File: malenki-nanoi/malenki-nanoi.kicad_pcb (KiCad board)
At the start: 4 copper layers, 19 x 32 mm, 45 parts, among them J1 Conn_01x02_Male-Connector, J2 Conn_01x08_Male, J3 Conn_01x02, J4 Conn_01x02_Male-Connector, J5 Conn_01x02_Male-Connector, J6 Conn_01x02_Male-Connector, U1 A7105, U2 AIC1734-33GUTR, U3 ATtiny1616-M, U4 DRV8837DSGR, U5 DRV8837DSGR, U6 DRV8837DSGR, Y1 16 Mhz 20ppm

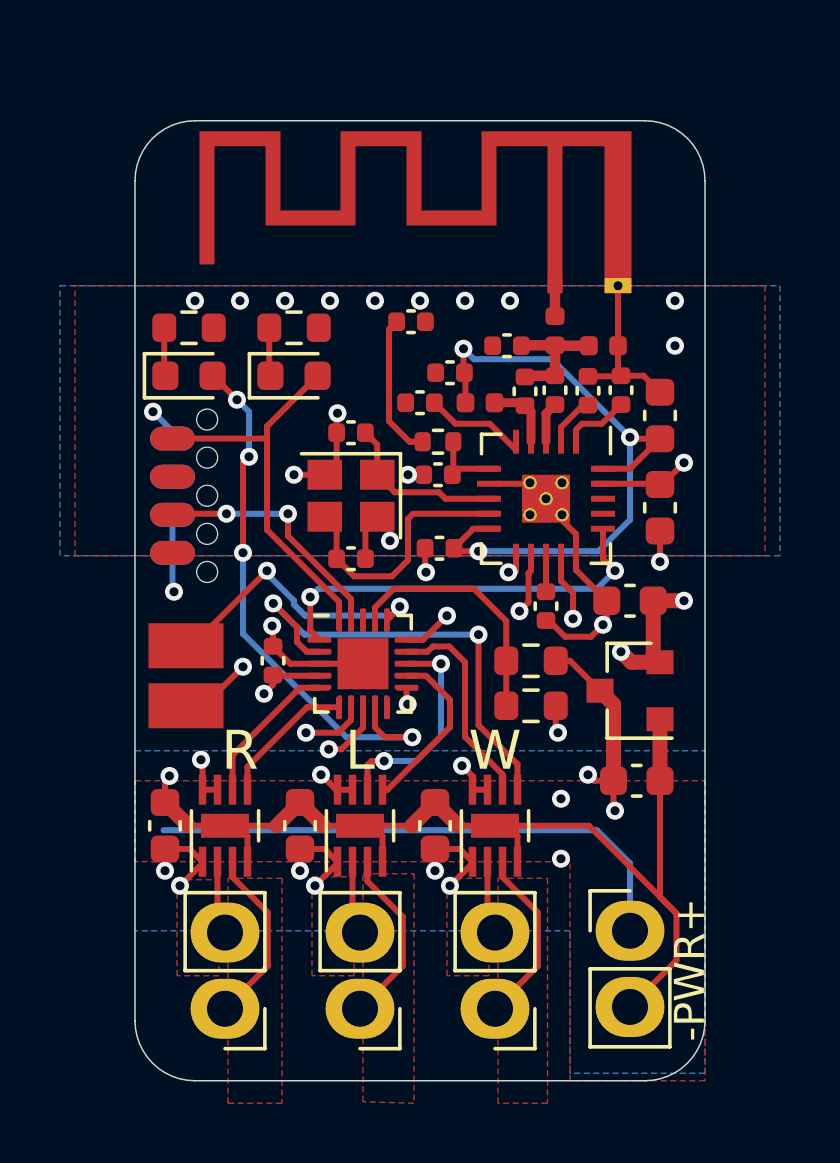
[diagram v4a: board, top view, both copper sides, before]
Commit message: Crystal caps update
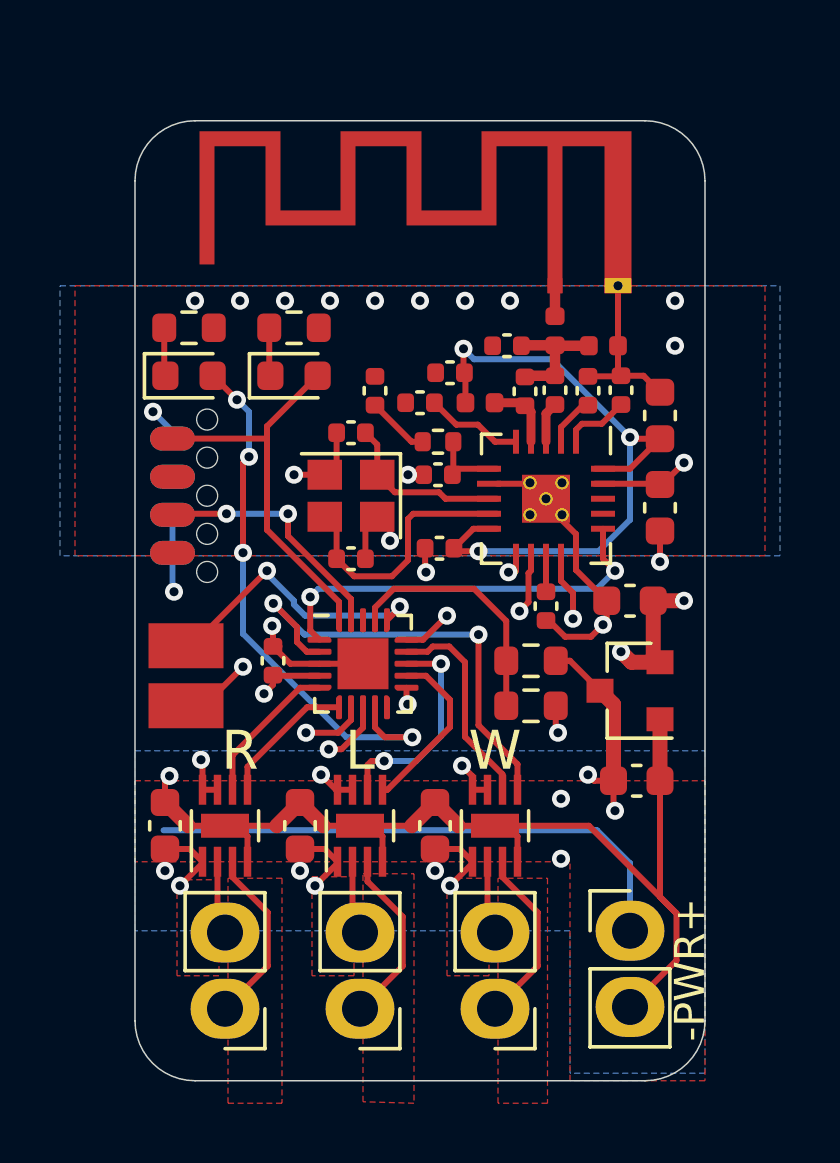
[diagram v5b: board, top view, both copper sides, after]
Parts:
- C14, C15: value 33pF -> 22pF
- R1, R2: value 100R -> 1k
- moved C19 2.59 mm to (96.0, 58.5), turned to 90 degrees
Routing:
- net Net-(C19-Pad1): track 4.83 -> 2.10 mm
- net GND: track 65.8 -> 65.1 mm, vias 23 -> 22
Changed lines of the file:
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@@
     (descr "Resistor SMD 0603 (1608 Metric), square (rectangular) end terminal, IPC_7351 nominal, (Body size source: IPC-SM-782 page 72, https://www.pcb-3d.com/wordpress/wp-content/uploads/ipc-sm-782a_amendment_1_and_2.pdf), generated with kicad-footprint-generator")
     (tags "resistor")
-    (property "LCSC" "C25804")
+    (property "LCSC" "")
     (property "Partnum" "C25804")
     (property "Sheet file" "malenki-nanoi.kicad_sch")
@@
       (effects (font (size 1 1) (thickness 0.15)))
     )
-    (fp_text value "33pF" (at 0 1.16) (layer "F.Fab")
+    (fp_text value "22pF" (at 0 1.16) (layer "F.Fab")
       (effects (font (size 1 1) (thickness 0.15)))
     )
@@
     (descr "Resistor SMD 0603 (1608 Metric), square (rectangular) end terminal, IPC_7351 nominal, (Body size source: IPC-SM-782 page 72, https://www.pcb-3d.com/wordpress/wp-content/uploads/ipc-sm-782a_amendment_1_and_2.pdf), generated with kicad-footprint-generator")
     (tags "resistor")
-    (property "LCSC" "C22775")
+    (property "LCSC" "")
     (property "Partnum" "")
     (property "Sheet file" "malenki-nanoi.kicad_sch")
@@
       (effects (font (size 1 1) (thickness 0.15)))
     )
-    (fp_text value "100R" (at 0 1.43) (layer "F.Fab") hide
+    (fp_text value "1k" (at 0 1.43) (layer "F.Fab") hide
       (effects (font (size 1 1) (thickness 0.15)))
     )
@@
       (effects (font (size 1 1) (thickness 0.15)))
     )
-    (fp_text value "33pF" (at 0 1.16) (layer "F.Fab")
+    (fp_text value "22pF" (at 0 1.16) (layer "F.Fab")
       (effects (font (size 1 1) (thickness 0.15)))
     )
@@
     (descr "Resistor SMD 0402 (1005 Metric), square (rectangular) end terminal, IPC_7351 nominal, (Body size source: IPC-SM-782 page 72, https://www.pcb-3d.com/wordpress/wp-content/uploads/ipc-sm-782a_amendment_1_and_2.pdf), generated with kicad-footprint-generator")
     (tags "resistor")
-    (property "LCSC" "C8218")
+    (property "LCSC" "")
     (property "Sheet file" "radio.kicad_sch")
     (property "Sheet name" "radio")
@@
     (descr "Resistor SMD 0603 (1608 Metric), square (rectangular) end terminal, IPC_7351 nominal, (Body size source: IPC-SM-782 page 72, https://www.pcb-3d.com/wordpress/wp-content/uploads/ipc-sm-782a_amendment_1_and_2.pdf), generated with kicad-footprint-generator")
     (tags "resistor")
-    (property "LCSC" "C4216")
+    (property "LCSC" "")
     (property "Partnum" "C4216")
     (property "Sheet file" "malenki-nanoi.kicad_sch")
@@
     (descr "Resistor SMD 0603 (1608 Metric), square (rectangular) end terminal, IPC_7351 nominal, (Body size source: IPC-SM-782 page 72, https://www.pcb-3d.com/wordpress/wp-content/uploads/ipc-sm-782a_amendment_1_and_2.pdf), generated with kicad-footprint-generator")
     (tags "resistor")
-    (property "LCSC" "C22775")
+    (property "LCSC" "")
     (property "Partnum" "")
     (property "Sheet file" "malenki-nanoi.kicad_sch")
@@
       (effects (font (size 1 1) (thickness 0.15)))
     )
-    (fp_text value "100R" (at 0 1.43) (layer "F.Fab") hide
+    (fp_text value "1k" (at 0 1.43) (layer "F.Fab") hide
       (effects (font (size 1 1) (thickness 0.15)))
     )
@@
   )
   (footprint "Capacitor_SMD:C_0402_1005Metric" (layer "F.Cu")
-    (at 97.2 56.2)
+    (at 96 58.5 90)
     (descr "Capacitor SMD 0402 (1005 Metric), square (rectangular) end terminal, IPC_7351 nominal, (Body size source: IPC-SM-782 page 76, https://www.pcb-3d.com/wordpress/wp-content/uploads/ipc-sm-782a_amendment_1_and_2.pdf), generated with kicad-footprint-generator")
     (tags "capacitor")
@@
     (property "Sheet name" "radio")
     (attr smd)
-    (fp_text reference "C19" (at 0 -1.16) (layer "F.SilkS") hide
-      (effects (font (size 1 1) (thickness 0.15)))
-    )
-    (fp_text value "10nF" (at 0 1.16) (layer "F.Fab")
-      (effects (font (size 1 1) (thickness 0.15)))
-    )
-    (fp_text user "${REFERENCE}" (at 0 0) (layer "F.Fab") hide
+    (fp_text reference "C19" (at 0 -1.16 90) (layer "F.SilkS") hide
+      (effects (font (size 1 1) (thickness 0.15)))
+    )
+    (fp_text value "10nF" (at 0 1.16 90) (layer "F.Fab")
+      (effects (font (size 1 1) (thickness 0.15)))
+    )
+    (fp_text user "${REFERENCE}" (at 0 0 90) (layer "F.Fab") hide
       (effects (font (size 0.25 0.25) (thickness 0.04)))
     )
@@
     (fp_line (start -0.5 0.25) (end -0.5 -0.25) (layer "F.Fab") (width 0.1))
     (fp_line (start 0.5 -0.25) (end 0.5 0.25) (layer "F.Fab") (width 0.1))
-    (pad "1" smd roundrect (at -0.48 0) (size 0.56 0.62) (layers "F.Cu" "F.Paste" "F.Mask") (roundrect_rratio 0.25)
+    (pad "1" smd roundrect (at -0.48 0 90) (size 0.56 0.62) (layers "F.Cu" "F.Paste" "F.Mask") (roundrect_rratio 0.25)
       (net 14 "Net-(C19-Pad1)"))
-    (pad "2" smd roundrect (at 0.48 0) (size 0.56 0.62) (layers "F.Cu" "F.Paste" "F.Mask") (roundrect_rratio 0.25)
+    (pad "2" smd roundrect (at 0.48 0 90) (size 0.56 0.62) (layers "F.Cu" "F.Paste" "F.Mask") (roundrect_rratio 0.25)
       (net 1 "GND"))
     (model "${KISYS3DMOD}/Capacitor_SMD.3dshapes/C_0402_1005Metric.wrl"
@@
   (segment (start 101.133334 61.6) (end 101.166667 61.566667) (width 0.2) (layer "F.Cu") (net 1))
   (segment (start 92.725 73) (end 93.5 72.225) (width 0.5) (layer "F.Cu") (net 1))
-  (segment (start 94.72 59.9) (end 94.72 59.28) (width 0.2) (layer "F.Cu") (net 1))
   (segment (start 103.2 66.7) (end 103.6 66.3) (width 0.2) (layer "F.Cu") (net 1))
   (segment (start 98.775 73) (end 100 73) (width 0.2) (layer "F.Cu") (net 1))
@@
   (segment (start 91.75 74.2) (end 91.75 73.35) (width 0.2) (layer "F.Cu") (net 1))
   (segment (start 93.18 67.6) (end 92.6 67.02) (width 0.2) (layer "F.Cu") (net 1))
-  (segment (start 94.72 59.28) (end 94.75 59.25) (width 0.2) (layer "F.Cu") (net 1))
   (segment (start 92.6 67.02) (end 92.82 67.02) (width 0.2) (layer "F.Cu") (net 1))
   (segment (start 106.05001 75.920097) (end 106.05001 77.48999) (width 0.2) (layer "F.Cu") (net 1))
@@
   (via (at 99 55.5) (size 0.6) (drill 0.3) (layers "F.Cu" "B.Cu") (free) (net 1))
   (via (at 91.5 55.5) (size 0.6) (drill 0.3) (layers "F.Cu" "B.Cu") (free) (net 1))
-  (via (at 94.75 59.25) (size 0.6) (drill 0.3) (layers "F.Cu" "B.Cu") (net 1))
   (via (at 105.5 64.2) (size 0.6) (drill 0.3) (layers "F.Cu" "B.Cu") (net 1))
   (via (at 102.1 69.9) (size 0.6) (drill 0.3) (layers "F.Cu" "B.Cu") (net 1))
@@
   (segment (start 104.5 60.05) (end 101.9 57.45) (width 0.2) (layer "B.Cu") (net 7))
   (segment (start 104.5 60.05) (end 104.5 62.8) (width 0.2) (layer "B.Cu") (net 7))
-  (segment (start 98.68 59.6) (end 97.98 58.9) (width 0.2) (layer "F.Cu") (net 8))
-  (segment (start 100.7 60.475) (end 99.825 59.6) (width 0.2) (layer "F.Cu") (net 8))
-  (segment (start 99.825 59.6) (end 98.68 59.6) (width 0.2) (layer "F.Cu") (net 8))
+  (segment (start 99.42999 59.62999) (end 98.70999 59.62999) (width 0.2) (layer "F.Cu") (net 8))
+  (segment (start 100.7 60.2) (end 100 60.2) (width 0.2) (layer "F.Cu") (net 8))
+  (segment (start 98.70999 59.62999) (end 97.98 58.9) (width 0.2) (layer "F.Cu") (net 8))
+  (segment (start 100 60.2) (end 99.42999 59.62999) (width 0.2) (layer "F.Cu") (net 8))
   (segment (start 96.56499 64.68501) (end 95.30501 64.68501) (width 0.2) (layer "F.Cu") (net 9))
   (segment (start 97.273086 62.6) (end 97.1 62.773086) (width 0.2) (layer "F.Cu") (net 9))
@@
   (segment (start 98.78 61.1) (end 98.58 61.3) (width 0.2) (layer "F.Cu") (net 13))
   (segment (start 98.61 60.2) (end 98.61 61.27) (width 0.2) (layer "F.Cu") (net 13))
-  (segment (start 97.15 60.2) (end 96.46499 59.51499) (width 0.2) (layer "F.Cu") (net 14))
-  (segment (start 96.46499 59.51499) (end 96.46499 56.45501) (width 0.2) (layer "F.Cu") (net 14))
-  (segment (start 97.59 60.2) (end 97.15 60.2) (width 0.2) (layer "F.Cu") (net 14))
-  (segment (start 96.46499 56.45501) (end 96.72 56.2) (width 0.2) (layer "F.Cu") (net 14))
+  (segment (start 97.59 60.2) (end 97.22 60.2) (width 0.2) (layer "F.Cu") (net 14))
+  (segment (start 97.22 60.2) (end 96 58.98) (width 0.2) (layer "F.Cu") (net 14))
   (segment (start 105.275 67.325) (end 105.5 67.55) (width 0.5) (layer "F.Cu") (net 15))
   (segment (start 105.5 61.625) (end 105.575 61.625) (width 0.2) (layer "F.Cu") (net 15))

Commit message: Use hand-solder footprints for all 0402
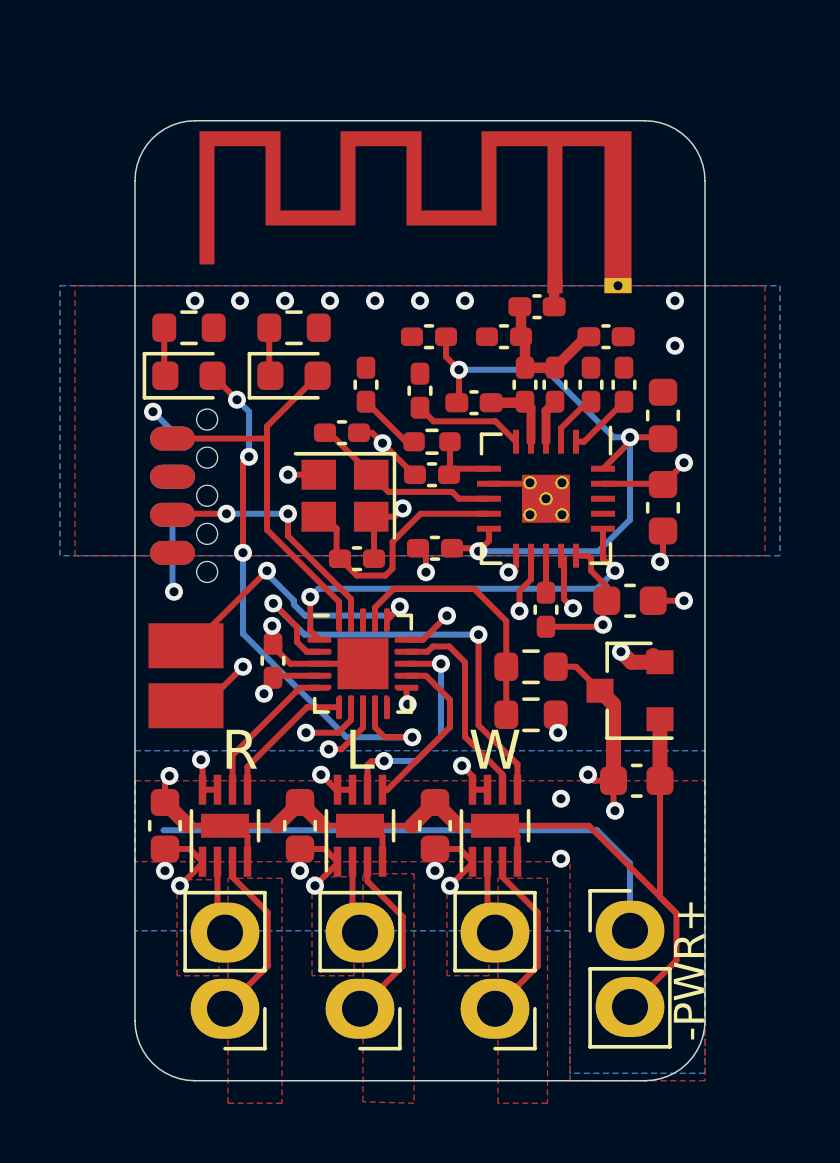
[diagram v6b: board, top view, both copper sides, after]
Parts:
- C10, C11, C12, C13, C14, C15, C16, C17, C18, C19, C22, C23, C4, C9: footprint Capacitor_SMD:C_0402_1005Metric -> Capacitor_SMD:C_0402_1005Metric_Pad0.74x0.62mm_HandSolder
- L1, L2, L3: footprint Inductor_SMD:L_0402_1005Metric -> Inductor_SMD:L_0402_1005Metric_Pad0.77x0.64mm_HandSolder
- R5: footprint Resistor_SMD:R_0402_1005Metric -> Resistor_SMD:R_0402_1005Metric_Pad0.72x0.64mm_HandSolder
- moved C12 1.39 mm to (97.8, 56.7)
- moved L1 1.00 mm to (101.4, 55.7), turned to 180 degrees
- moved C13 0.40 mm to (97.5, 58.5), turned to 90 degrees
- moved C19 0.36 mm to (95.7, 58.3)
- moved C9 0.32 mm to (100.3, 56.7)
- moved L2 0.31 mm to (103.7, 56.7)
- moved C15 0.30 mm to (94.9, 59.9), turned to 0 degrees
- moved R4 0.30 mm to (101.2, 69.3)
- moved C17 0.22 mm to (103.2, 58.3)
- moved C11 0.22 mm to (101.0, 58.3)
- moved C16 0.21 mm to (104.3, 58.3)
- moved C14 0.20 mm to (95.4, 64.1)
- moved L3 0.20 mm to (99.3, 58.9)
- moved R3 0.20 mm to (101.2, 67.7)
- moved Y1 0.20 mm to (95.0, 62.0)
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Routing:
- net GND: track 65.1 -> 58.3 mm, vias 22 -> 21
- net VLOGIC: track 14.4 -> 12.3 mm
- net /radio/REGOA: track 23.0 -> 21.6 mm
- net SPI_SCS: track 8.40 -> 7.62 mm
- net SPI_SDIO: track 17.0 -> 16.2 mm
- net Net-(C14-Pad1): track 8.83 -> 8.14 mm

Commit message: update some comments pin1 marks on silkscreen
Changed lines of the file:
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@@
       (net 17 "TXDEBUG") (pinfunction "Pin_8"))
   )
+  (gr_circle (center 98.5 74.5) (end 98.75 74.5) (layer "F.SilkS") (width 0.12) (fill solid))
+  (gr_circle (center 93.2 66) (end 93.45 66) (layer "F.SilkS") (width 0.12) (fill solid))
+  (gr_circle (center 96.5 59.8) (end 96.75 59.8) (layer "F.SilkS") (width 0.12) (fill solid))
+  (gr_circle (center 94.1 74.5) (end 94.35 74.5) (layer "F.SilkS") (width 0.12) (fill solid))
+  (gr_circle (center 89.6 74.5) (end 89.85 74.5) (layer "F.SilkS") (width 0.12) (fill solid))
+  (gr_circle (center 104.2 59.6) (end 104.45 59.6) (layer "F.SilkS") (width 0.12) (fill solid))
   (gr_arc (start 90 51.5) (end 90 49.5) (angle -90) (layer "Edge.Cuts") (width 0.05))
   (gr_line (start 90 49.5) (end 105 49.5) (layer "Edge.Cuts") (width 0.05))
